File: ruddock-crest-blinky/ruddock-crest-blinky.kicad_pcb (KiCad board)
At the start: 2 copper layers, 38.1 x 45.7 mm, 30 parts, among them J1 JST PH, Q1 NMOSFET, SW1 SW_SPDT, SW2 SW_USER, U1 ATtiny85-20SU, U2 74HC595

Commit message: Choose polarity protection MOSFET
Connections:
- J1 pad 1: Net-(BT1-Pad1) -> Net-(BT1-Pad2)
- J1 pad 2: Net-(BT1-Pad2) -> Net-(BT1-Pad1)
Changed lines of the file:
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@@
     )
     (pad 1 smd roundrect (at -1 0.5 180) (size 1 5.5) (layers F.Cu F.Paste F.Mask) (roundrect_rratio 0.25)
+      (net 1 "Net-(BT1-Pad2)"))
+    (pad 2 smd roundrect (at 1 0.5 180) (size 1 5.5) (layers F.Cu F.Paste F.Mask) (roundrect_rratio 0.25)
       (net 2 "Net-(BT1-Pad1)"))
-    (pad 2 smd roundrect (at 1 0.5 180) (size 1 5.5) (layers F.Cu F.Paste F.Mask) (roundrect_rratio 0.25)
-      (net 1 "Net-(BT1-Pad2)"))
     (pad MP smd roundrect (at -3.4 -1.75 180) (size 1.6 3) (layers F.Cu F.Paste F.Mask) (roundrect_rratio 0.15625))
     (pad MP smd roundrect (at 3.4 -1.75 180) (size 1.6 3) (layers F.Cu F.Paste F.Mask) (roundrect_rratio 0.15625))

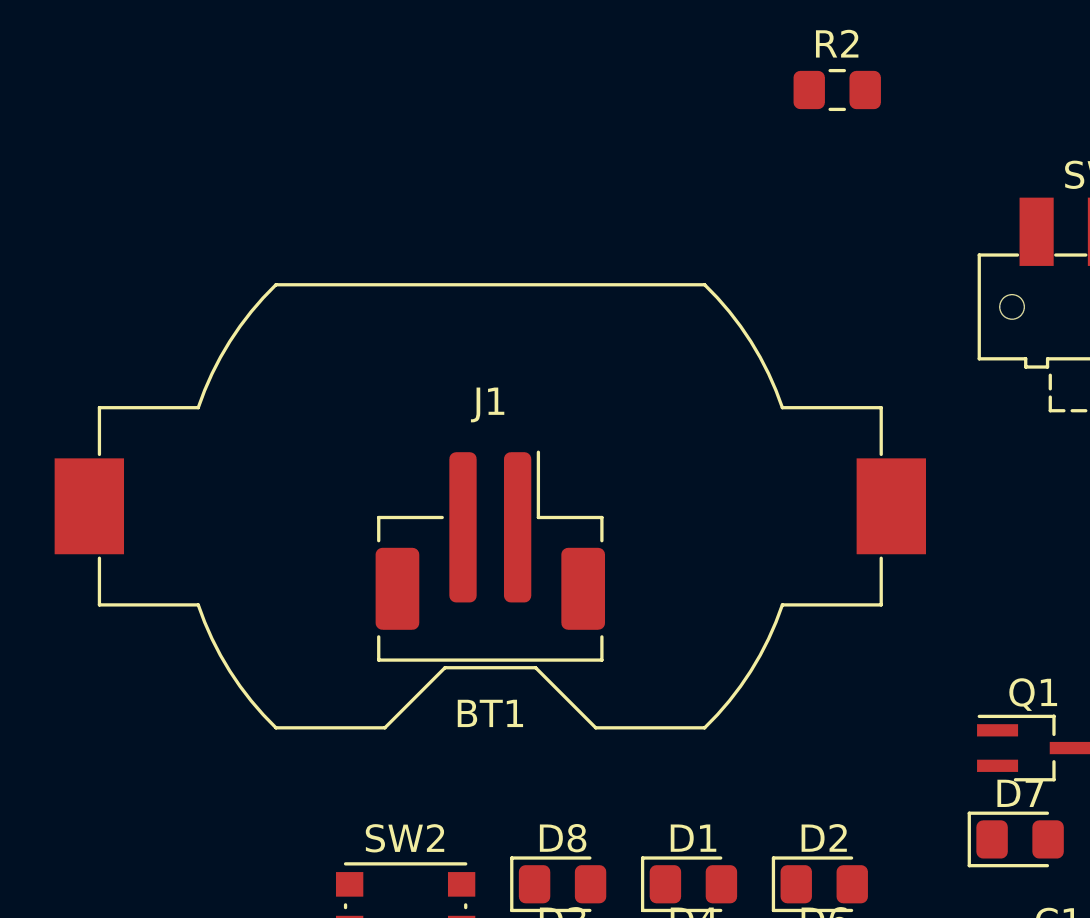
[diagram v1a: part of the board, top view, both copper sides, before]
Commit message: Select battery holder and switches
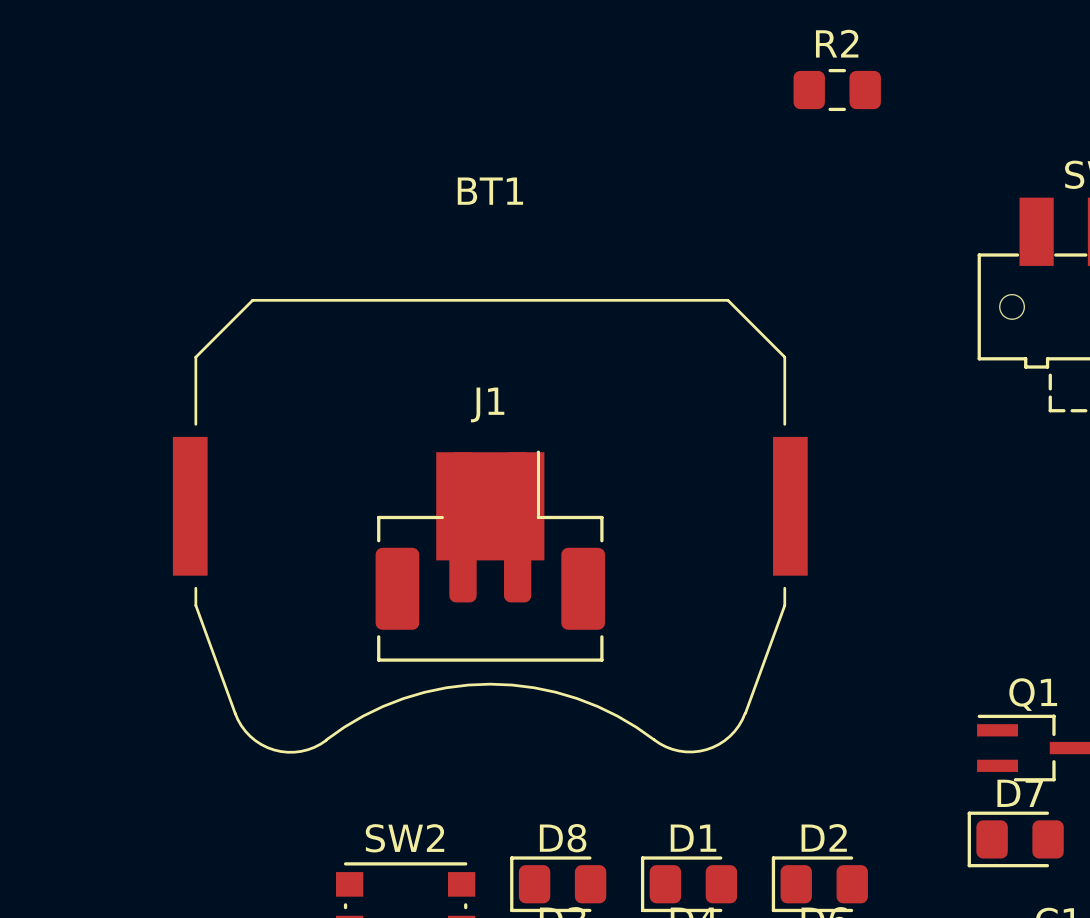
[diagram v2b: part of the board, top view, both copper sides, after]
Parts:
- BT1: footprint Battery:BatteryHolder_Keystone_1058_1x2032 -> Battery:BatteryHolder_Keystone_3034_1x20mm
- C4: value 0.1uF -> 1uF
- Q1: value NMOSFET -> DMN2058UW
- SW1: value SW_SPDT -> JS102011JCQN

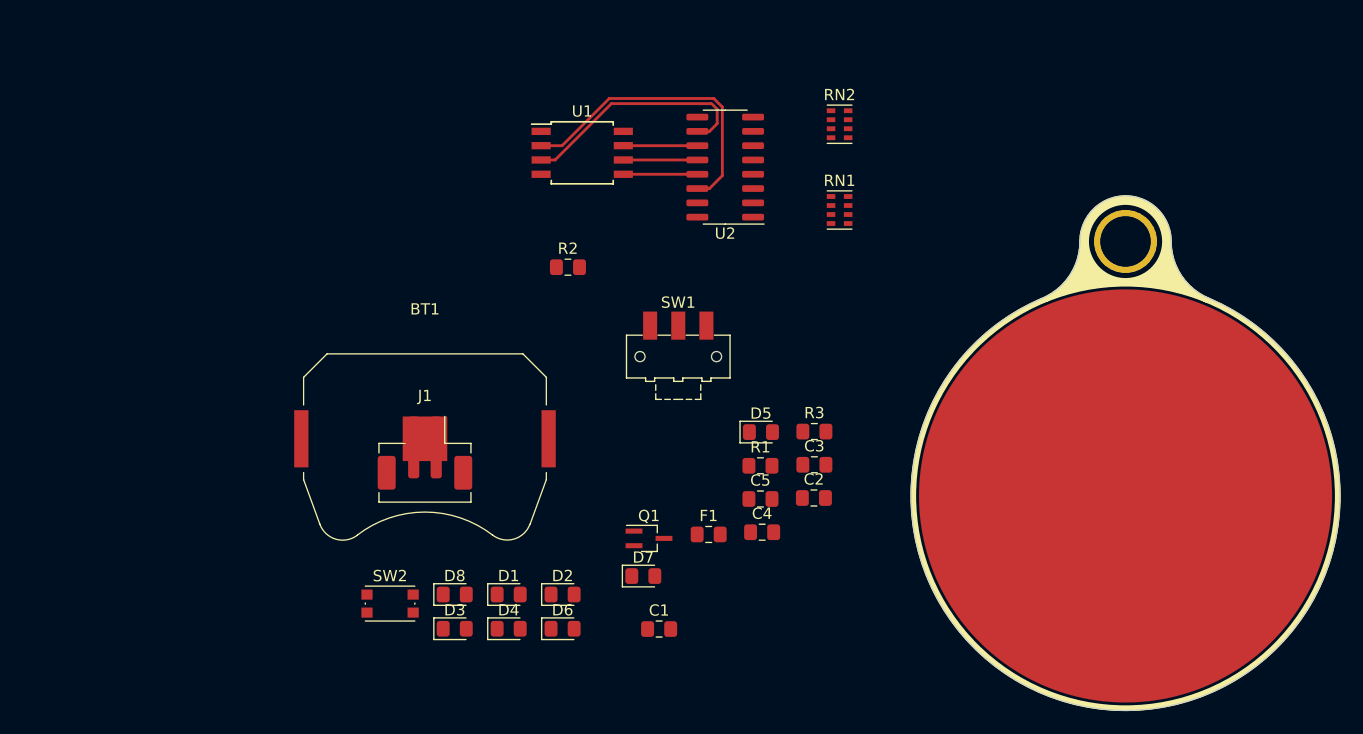
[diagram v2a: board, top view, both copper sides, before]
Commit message: Replace resistor packs with discrete resistors
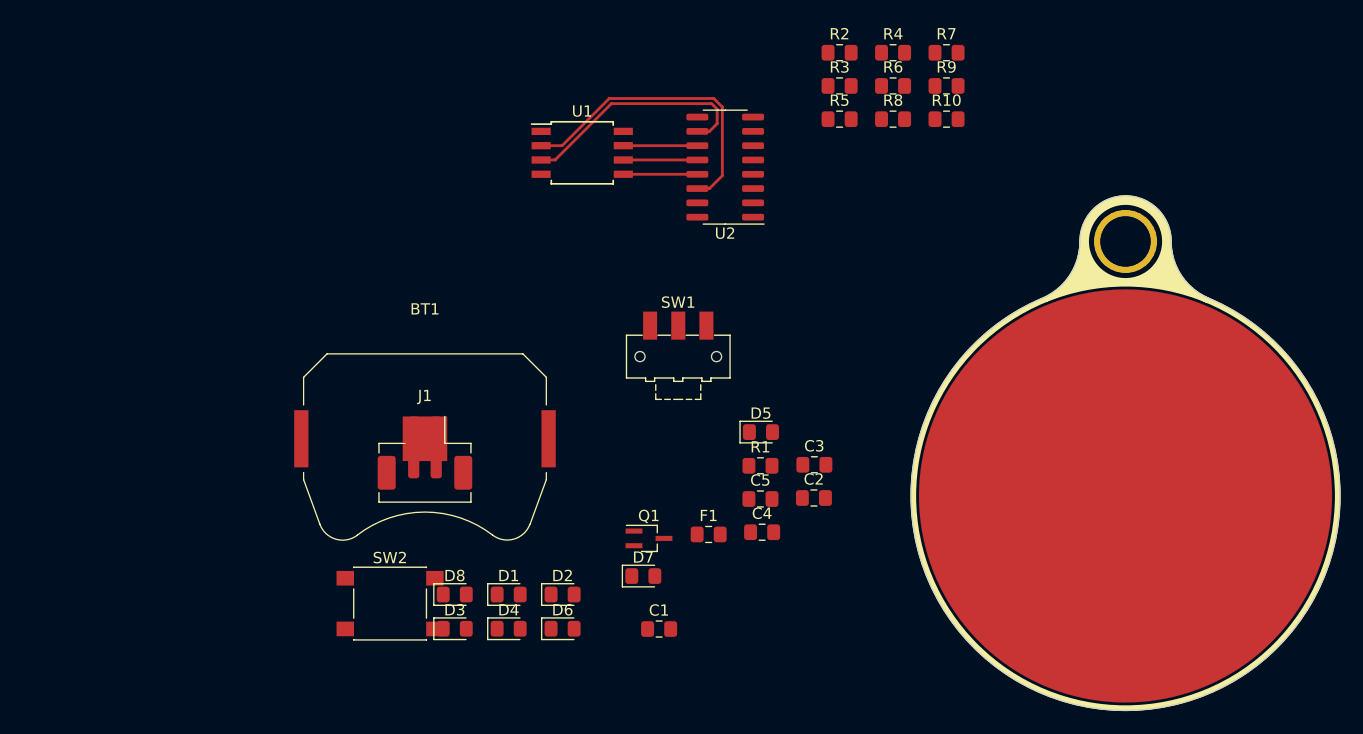
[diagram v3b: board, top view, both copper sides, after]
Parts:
- removed RN1, RN2: 100, Resistor_SMD:R_Cat16-4
- added R10: 10K, Resistor_SMD:R_0805_2012Metric_Pad1.15x1.40mm_HandSolder, F.Cu at (125.1, 74.5)
- added R4: R, Resistor_SMD:R_0805_2012Metric_Pad1.15x1.40mm_HandSolder, F.Cu at (120.3, 68.6)
- added R5: R, Resistor_SMD:R_0805_2012Metric_Pad1.15x1.40mm_HandSolder, F.Cu at (115.6, 74.5)
- added R6: R, Resistor_SMD:R_0805_2012Metric_Pad1.15x1.40mm_HandSolder, F.Cu at (120.3, 71.5)
- added R7: R, Resistor_SMD:R_0805_2012Metric_Pad1.15x1.40mm_HandSolder, F.Cu at (125.1, 68.6)
- added R8: R, Resistor_SMD:R_0805_2012Metric_Pad1.15x1.40mm_HandSolder, F.Cu at (120.3, 74.5)
- added R9: R, Resistor_SMD:R_0805_2012Metric_Pad1.15x1.40mm_HandSolder, F.Cu at (125.1, 71.5)
- R2, R3: value 10K -> R
- SW2: value SW_USER -> PTS 647 SK38 SMTR2 LFS; footprint Button_Switch_SMD:SW_Push_1P1T_NO_CK_KMR2 -> Button_Switch_SMD:SW_SPST_PTS645
- moved R3 30.8 mm to (115.6, 71.5)
- moved R2 30.7 mm to (115.6, 68.6)
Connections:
- R2 pad 1: VCC -> Net-(R2-Pad1)
- R2 pad 2: Net-(R2-Pad2) -> Net-(D1-Pad2)
- R3 pad 1: VCC -> Net-(R3-Pad1)
- R3 pad 2: Net-(C5-Pad1) -> Net-(D2-Pad2)
- U2 pad 1: Net-(RN1-Pad3) -> Net-(R3-Pad1)
- U2 pad 15: Net-(RN1-Pad4) -> Net-(R2-Pad1)

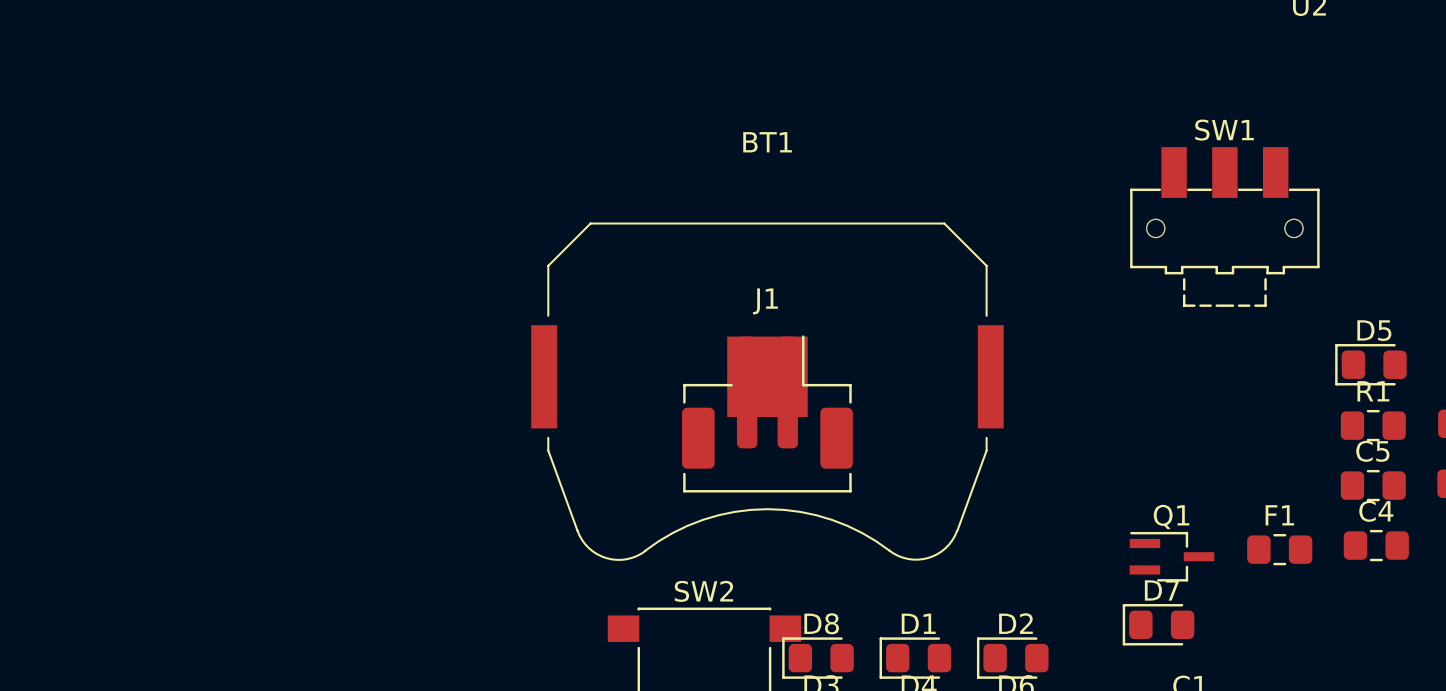
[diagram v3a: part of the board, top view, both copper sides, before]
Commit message: Select fuse
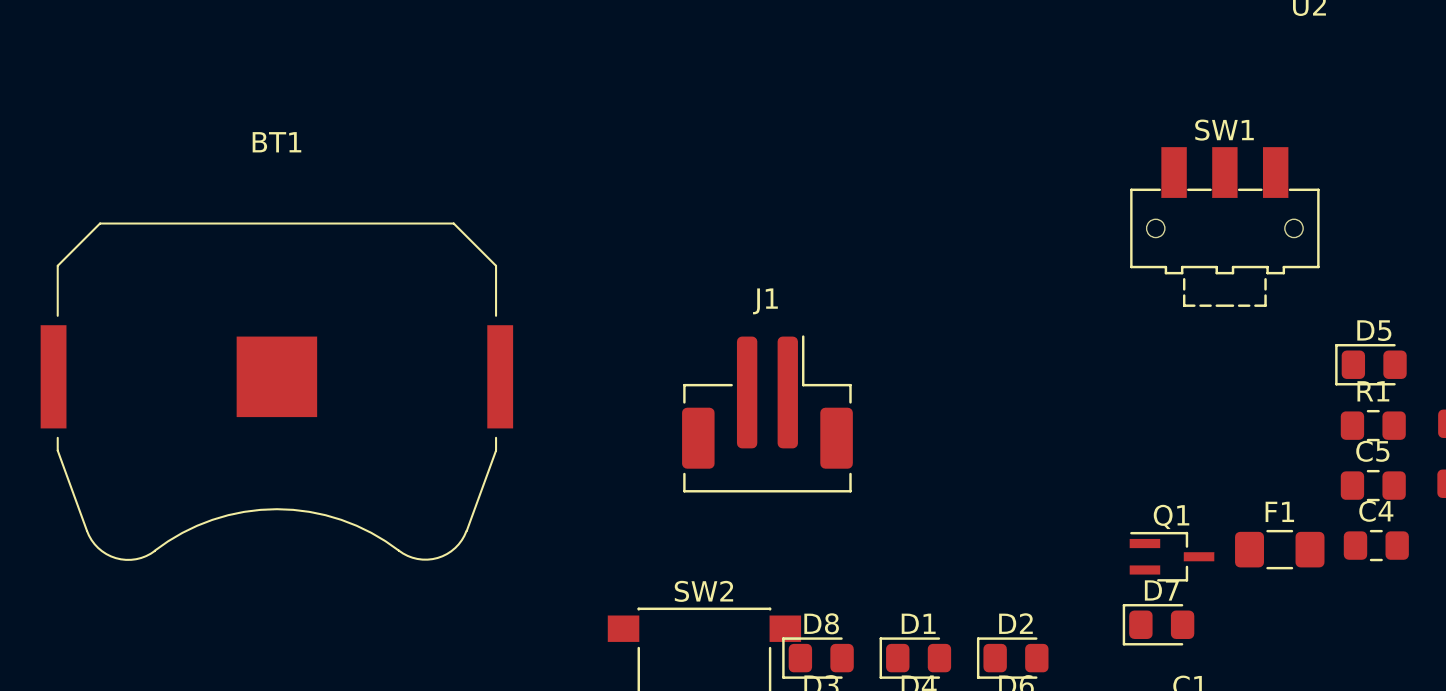
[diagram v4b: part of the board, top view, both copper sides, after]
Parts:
- F1: value Fuse_Small -> 0ZCJ0005FF2E; footprint Fuse:Fuse_0805_2012Metric_Pad1.15x1.40mm_HandSolder -> Fuse:Fuse_1206_3216Metric_Pad1.42x1.75mm_HandSolder
- moved BT1 24.1 mm to (54.6, 102.9)
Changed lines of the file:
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@@
     (add_net VCC)
+  )
+  (module Fuse:Fuse_1206_3216Metric_Pad1.42x1.75mm_HandSolder (layer F.Cu)
+    (at 103.94 111.37103)
+    (descr "Fuse SMD 1206 (3216 Metric), square (rectangular) end terminal, IPC_7351 nominal with elongated pad for handsoldering. (Body size source: http://www.tortai-tech.com/upload/download/2011102023233369053.pdf), generated with kicad-footprint-generator")
+    (tags "resistor handsolder")
+    (attr smd)
+    (fp_text reference F1 (at 0 -1.82) (layer F.SilkS)
+      (effects (font (size 1 1) (thickness 0.15)))
+    )
+    (fp_text value " 0ZCJ0005FF2E " (at 0 1.82) (layer F.Fab)
+      (effects (font (size 1 1) (thickness 0.15)))
+    )
+    (fp_text user %R (at 0 0) (layer F.Fab)
+      (effects (font (size 0.8 0.8) (thickness 0.12)))
+    )
+    (fp_line (start 2.45 1.12) (end -2.45 1.12) (layer F.CrtYd) (width 0.05))
+    (fp_line (start 2.45 -1.12) (end 2.45 1.12) (layer F.CrtYd) (width 0.05))
+    (fp_line (start -2.45 -1.12) (end 2.45 -1.12) (layer F.CrtYd) (width 0.05))
+    (fp_line (start -2.45 1.12) (end -2.45 -1.12) (layer F.CrtYd) (width 0.05))
+    (fp_line (start -0.602064 0.91) (end 0.602064 0.91) (layer F.SilkS) (width 0.12))
+    (fp_line (start -0.602064 -0.91) (end 0.602064 -0.91) (layer F.SilkS) (width 0.12))
+    (fp_line (start 1.6 0.8) (end -1.6 0.8) (layer F.Fab) (width 0.1))
+    (fp_line (start 1.6 -0.8) (end 1.6 0.8) (layer F.Fab) (width 0.1))
+    (fp_line (start -1.6 -0.8) (end 1.6 -0.8) (layer F.Fab) (width 0.1))
+    (fp_line (start -1.6 0.8) (end -1.6 -0.8) (layer F.Fab) (width 0.1))
+    (pad 2 smd roundrect (at 1.4875 0) (size 1.425 1.75) (layers F.Cu F.Paste F.Mask) (roundrect_rratio 0.175439)
+      (net 14 "Net-(F1-Pad2)"))
+    (pad 1 smd roundrect (at -1.4875 0) (size 1.425 1.75) (layers F.Cu F.Paste F.Mask) (roundrect_rratio 0.175439)
+      (net 2 "Net-(BT1-Pad1)"))
+    (model ${KISYS3DMOD}/Fuse.3dshapes/Fuse_1206_3216Metric.wrl
+      (at (xyz 0 0 0))
+      (scale (xyz 1 1 1))
+      (rotate (xyz 0 0 0))
+    )
   )
   (module Button_Switch_SMD:SW_SPST_PTS645 (layer F.Cu)
@@
   )
   (module Battery:BatteryHolder_Keystone_3034_1x20mm (layer F.Cu)
-    (at 78.74 102.87)
+    (at 54.61 102.87)
     (descr "Keystone 3034 SMD battery holder for 2020, 2025 and 2032 coincell batteries. http://www.keyelco.com/product-pdf.cfm?p=798")
     (tags "Keystone type 3034 coin cell retainer")
@@
       (at (xyz 0 0 0))
       (scale (xyz 1 1 1))
-      (rotate (xyz 0 0 0))
-    )
-  )
-  (module Fuse:Fuse_0805_2012Metric_Pad1.15x1.40mm_HandSolder (layer F.Cu)
-    (at 103.94 111.37103)
-    (descr "Fuse SMD 0805 (2012 Metric), square (rectangular) end terminal, IPC_7351 nominal with elongated pad for handsoldering. (Body size source: https://docs.google.com/spreadsheets/d/1BsfQQcO9C6DZCsRaXUlFlo91Tg2WpOkGARC1WS5S8t0/edit?usp=sharing), generated with kicad-footprint-generator")
-    (tags "resistor handsolder")
-    (attr smd)
-    (fp_text reference F1 (at 0 -1.65) (layer F.SilkS)
-      (effects (font (size 1 1) (thickness 0.15)))
-    )
-    (fp_text value Fuse_Small (at 0 1.65) (layer F.Fab)
-      (effects (font (size 1 1) (thickness 0.15)))
-    )
-    (fp_text user %R (at 0 0) (layer F.Fab)
-      (effects (font (size 0.5 0.5) (thickness 0.08)))
-    )
-    (fp_line (start 1.85 0.95) (end -1.85 0.95) (layer F.CrtYd) (width 0.05))
-    (fp_line (start 1.85 -0.95) (end 1.85 0.95) (layer F.CrtYd) (width 0.05))
-    (fp_line (start -1.85 -0.95) (end 1.85 -0.95) (layer F.CrtYd) (width 0.05))
-    (fp_line (start -1.85 0.95) (end -1.85 -0.95) (layer F.CrtYd) (width 0.05))
-    (fp_line (start -0.261252 0.71) (end 0.261252 0.71) (layer F.SilkS) (width 0.12))
-    (fp_line (start -0.261252 -0.71) (end 0.261252 -0.71) (layer F.SilkS) (width 0.12))
-    (fp_line (start 1 0.6) (end -1 0.6) (layer F.Fab) (width 0.1))
-    (fp_line (start 1 -0.6) (end 1 0.6) (layer F.Fab) (width 0.1))
-    (fp_line (start -1 -0.6) (end 1 -0.6) (layer F.Fab) (width 0.1))
-    (fp_line (start -1 0.6) (end -1 -0.6) (layer F.Fab) (width 0.1))
-    (pad 2 smd roundrect (at 1.025 0) (size 1.15 1.4) (layers F.Cu F.Paste F.Mask) (roundrect_rratio 0.217391)
-      (net 14 "Net-(F1-Pad2)"))
-    (pad 1 smd roundrect (at -1.025 0) (size 1.15 1.4) (layers F.Cu F.Paste F.Mask) (roundrect_rratio 0.217391)
-      (net 2 "Net-(BT1-Pad1)"))
-    (model ${KISYS3DMOD}/Fuse.3dshapes/Fuse_0805_2012Metric.wrl
-      (at (xyz 0 0 0))
-      (scale (xyz 1 1 1))
